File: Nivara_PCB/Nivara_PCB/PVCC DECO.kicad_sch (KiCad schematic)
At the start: 3 parts, among them SW3 SW_Push

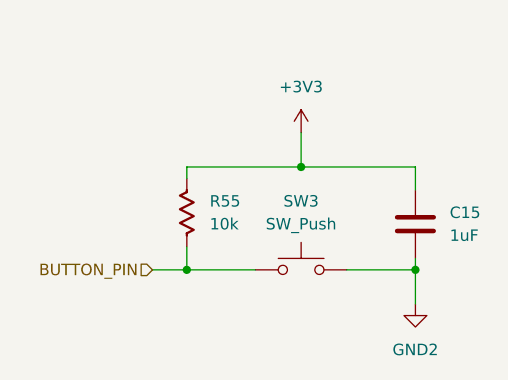
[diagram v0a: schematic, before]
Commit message: Cambios en las silscreen de los componentes.
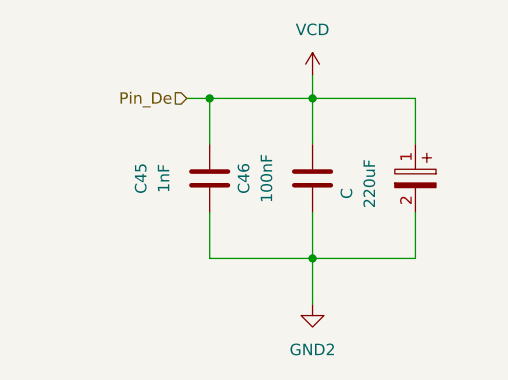
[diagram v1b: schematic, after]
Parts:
- removed C15: 1uF, PCM_Capacitor_SMD_AKL:C_0603_1608Metric, symbol EasyEDA:C_0603
- removed R55: 10k, PCM_Resistor_SMD_AKL:R_0603_1608Metric, symbol EasyEDA:R_0603
- removed SW3: SW_Push, Button_Switch_SMD:SW_SPST_PTS810, symbol Switch:SW_Push
- added C: 220uF, EasyEDA2:CAP-SMD_BD10.0-L10.3-W10.3-LS11.0-FD, symbol EasyEDA2:C_Polarized_220uF_63V
- added C45: 1nF, PCM_Capacitor_SMD_AKL:C_0603_1608Metric, symbol PCM_Capacitor_US_AKL:C_0603
- added C46: 100nF, PCM_Capacitor_SMD_AKL:C_0805_2012Metric, symbol EasyEDA:C_0805
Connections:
- net GND2: now also C.2, C45.2, C46.1
- new net VCD: C.1, C45.1, C46.2
